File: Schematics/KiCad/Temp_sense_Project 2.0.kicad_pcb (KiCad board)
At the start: 2 copper layers, 220 x 99 mm, 197 parts, among them J1 348260240, J10 348260240, J11 348260240, J13 348260240, J2 348260240, J3 348260240, J4 348260240, J5 348260240, J6 348260240, J7 Conn_02x08_Odd_Even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

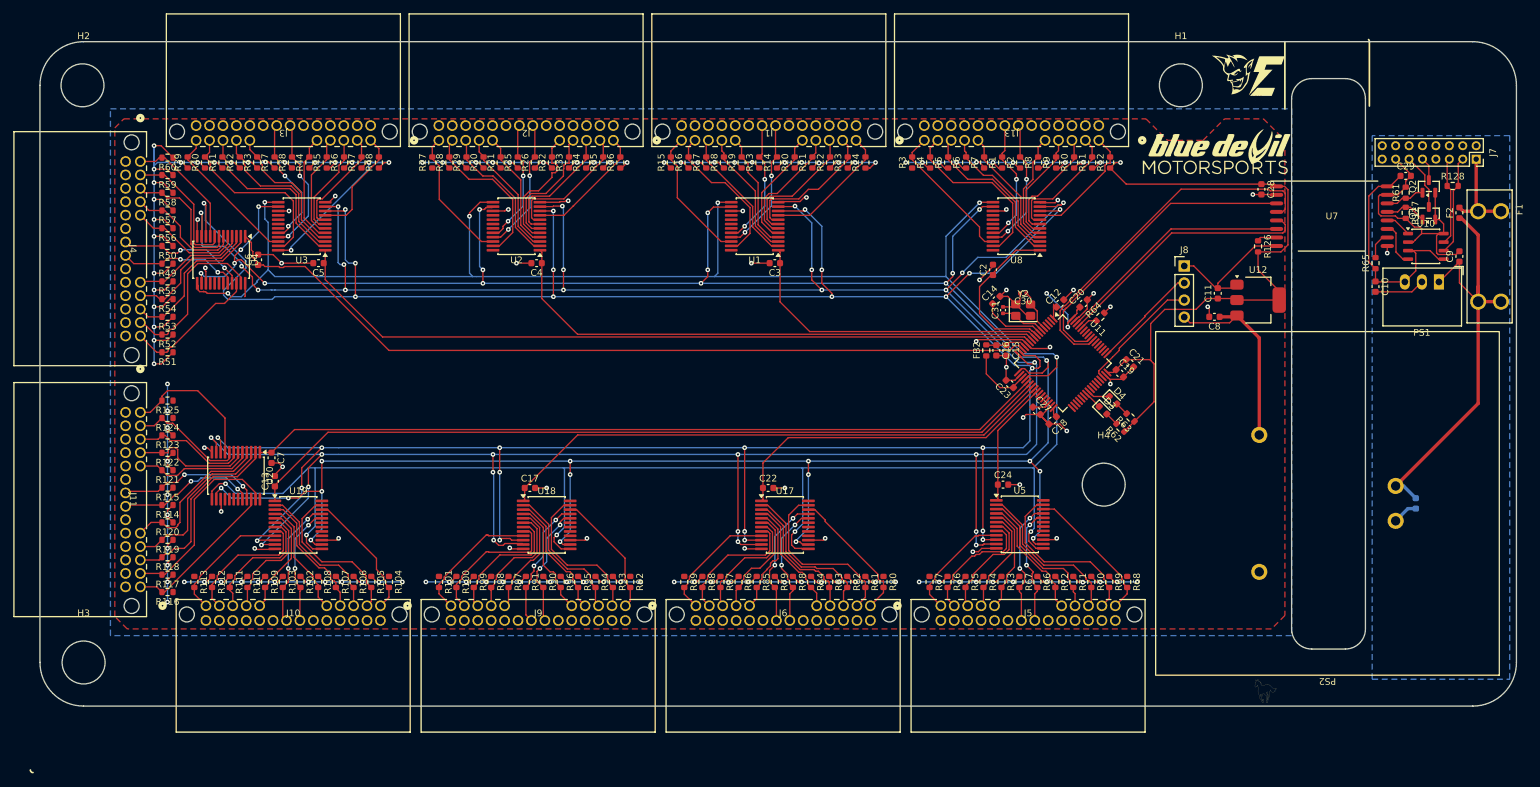
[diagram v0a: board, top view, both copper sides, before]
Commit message: Move some silkscreen around
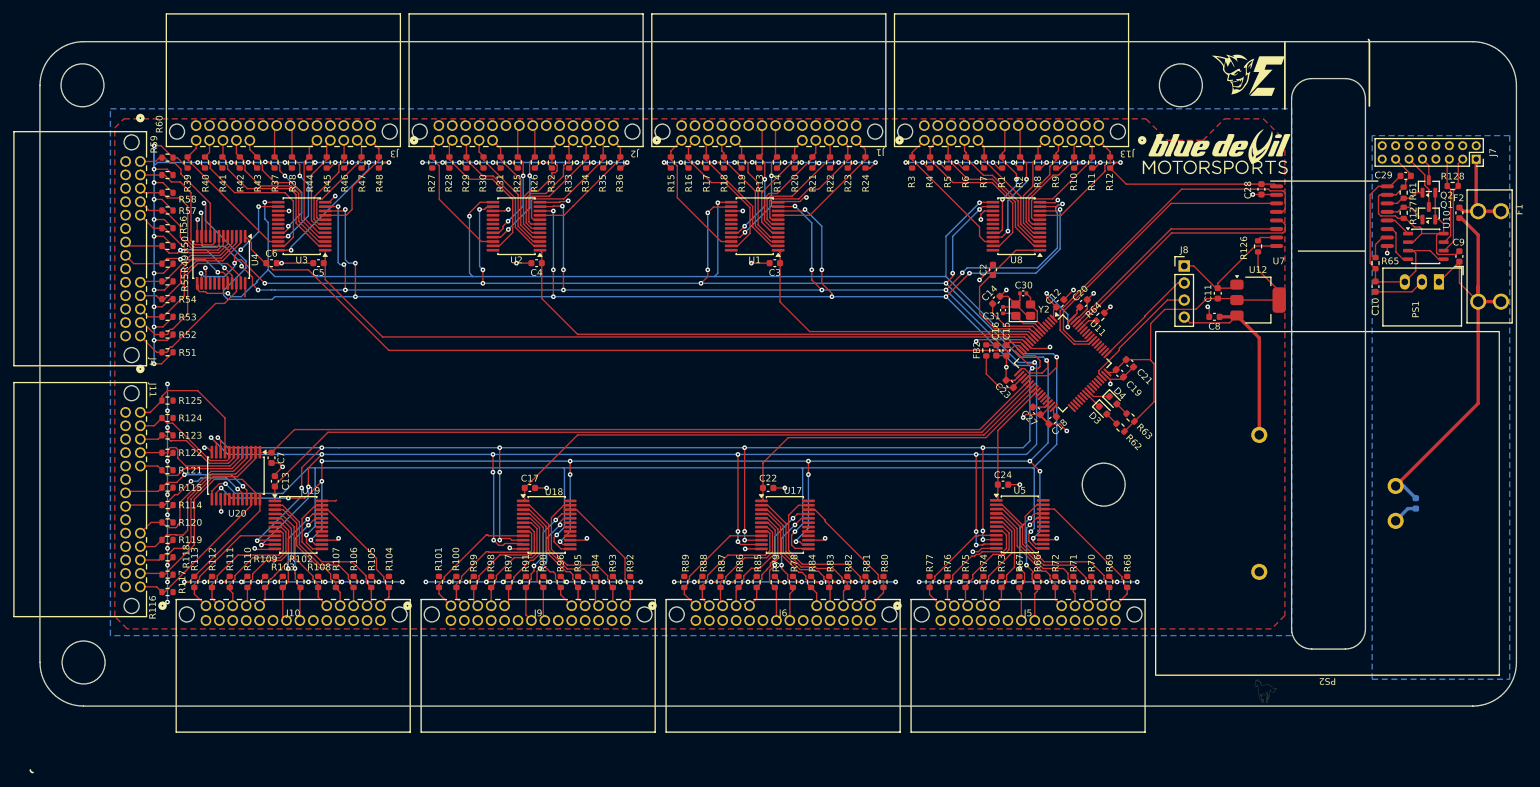
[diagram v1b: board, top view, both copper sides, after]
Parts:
- moved C6 2.06 mm to (81.4, 83.8), turned to 0 degrees
- moved R127 0.30 mm to (250.1, 76.3)
- moved R61 0.30 mm to (250.1, 73.3)
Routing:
- net +3V3: track 659.5 -> 667.5 mm, vias 120 -> 119
- net /MCU/S0: track 435.6 -> 439.1 mm
- net /MCU/S1: track 428.7 -> 432.1 mm
- net GND: track 159.8 -> 156.3 mm
- net /MCU/MUX 9: track 124.9 -> 124.0 mm
- net Net-(U4-I1): track 19.9 -> 20.6 mm
- net /MCU/S2: track 396.0 -> 396.6 mm
